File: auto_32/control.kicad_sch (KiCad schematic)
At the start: 12 parts, among them SW1 SW_Push, Y1 Crystal

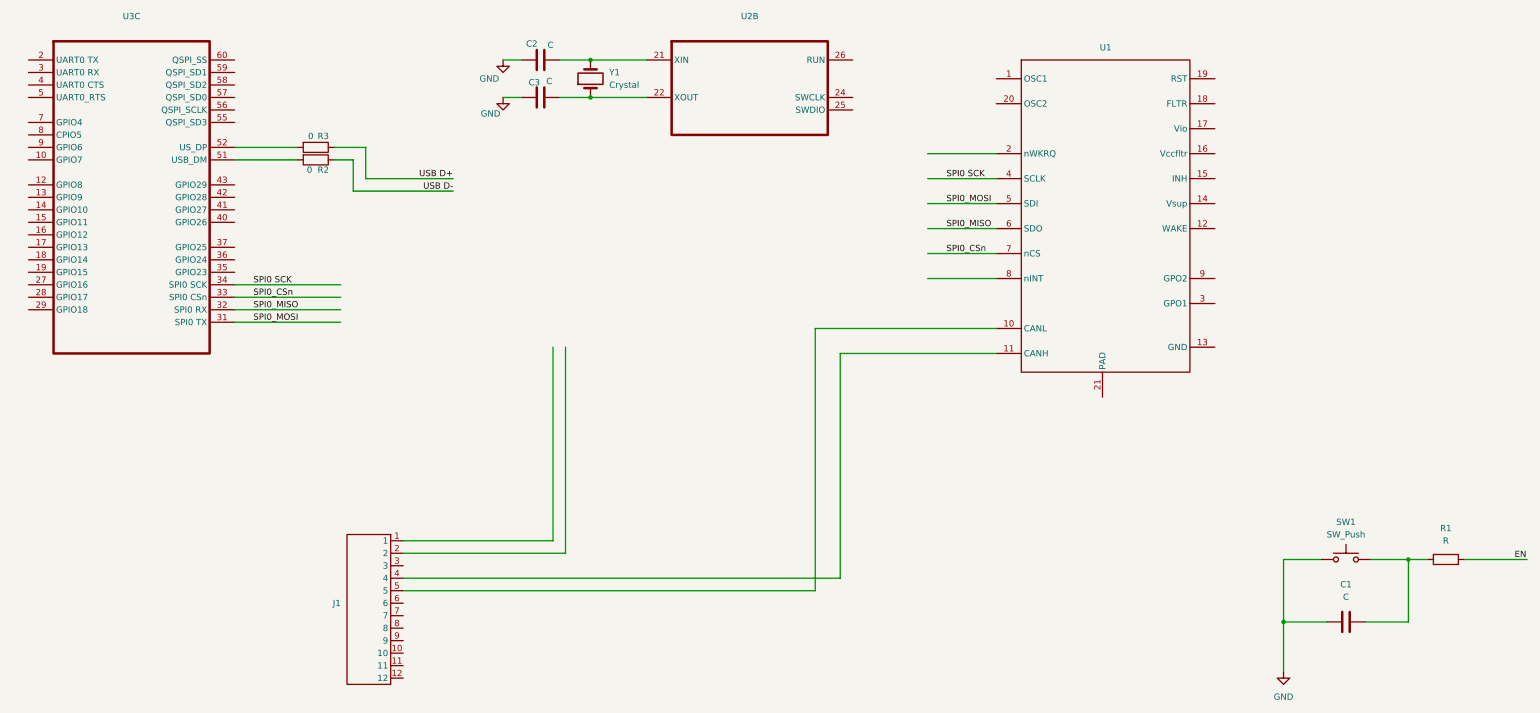
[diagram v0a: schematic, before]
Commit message: esp wroom reintroduced and can phy layer chip added
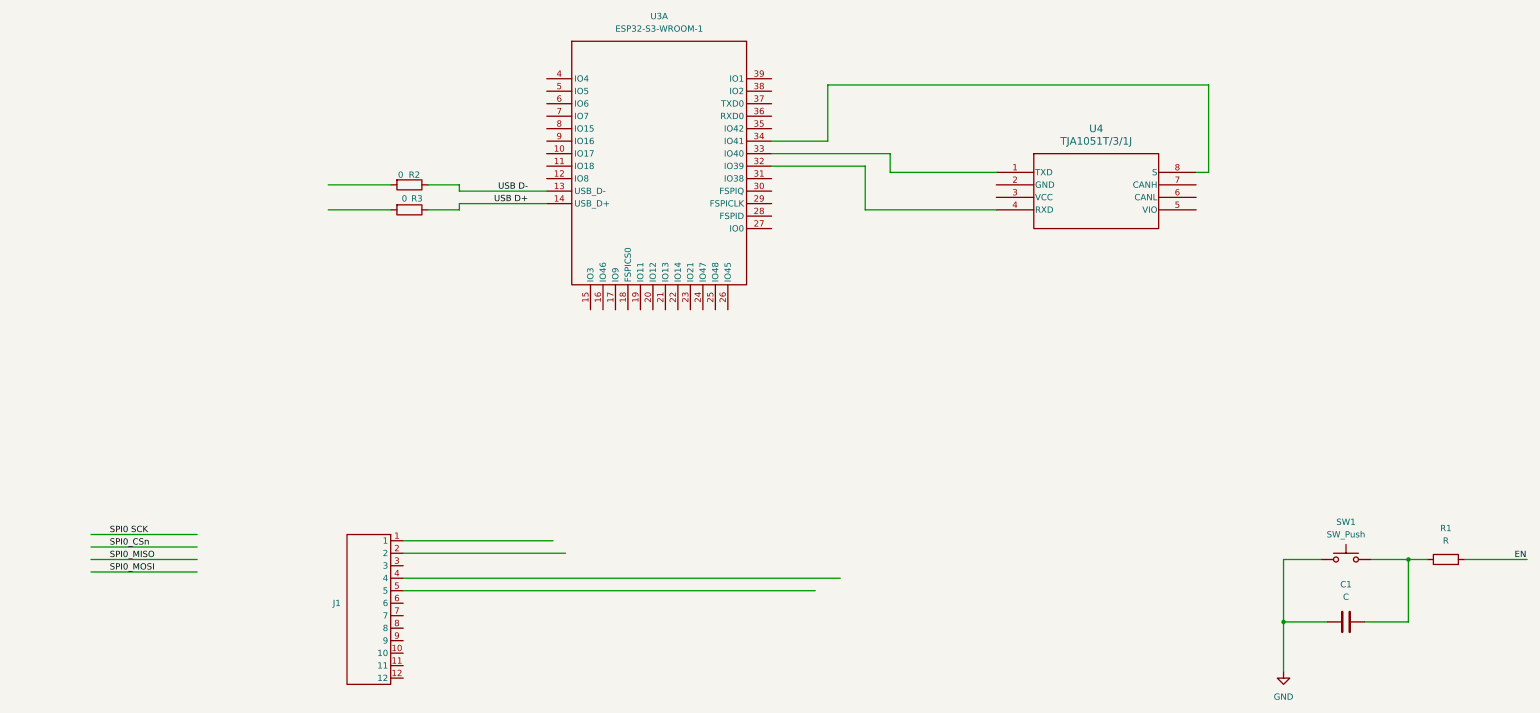
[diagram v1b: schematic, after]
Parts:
- removed C2: C, Capacitor_SMD:C_0603_1608Metric, symbol Device:C
- removed C3: C, symbol Device:C
- removed U1: ~, ssh_Library:VQFN-26_EP_3.5x4.5_Pitch0.5mm, symbol ssh_Library:TCAN4551RGYRQ1
- removed U2, U3: ~, ssh_IC_FP:RP2350A_QFN-60_EP_7.75x7.75_Pitch0.4mm, symbol ssh_IC_Lib:rp2050A_60pin
- removed Y1: Crystal, symbol Device:Crystal
- added U3: ESP32-S3-WROOM-1, RF_Module:ESP32-S3-WROOM-1, symbol ssh_Library:ESP32-S3-WROOM-1
- added U4: TJA1051T/3/1J, ssh_IC_FP:SO8_SOT96-1_NXP, symbol ssh_IC_Lib:TJA1051T_3_1J
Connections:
- net USB D+: now also U3.14 (IO20)
- net USB D-: now also U3.13 (IO19)
- new net: U3.32 (IO39), U4.4 (RXD)
- new net: U3.33 (IO40), U4.1 (TXD)
- new net: U3.34 (IO41), U4.8 (S)
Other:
- moved on the sheet: R2, R3

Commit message: march update
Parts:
- removed C1: C, symbol Device:C
- removed R1: R, symbol Device:R
- removed SW1: SW_Push, symbol Switch:SW_Push
- added C?: 4n7F, symbol Device:C
- added R? (x2): 60R, symbol Device:R
- renumbered R2 to R4, R3 to R5, U3 to U2, U4 to U3
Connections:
- net GND: now also U3.2 (GND), C?.2
- net CANH: now reaches J1.4
- net CANH: now also U3.7 (CANH), R?.2
- net CANL: now reaches J1.5
- net CANL: now also U3.6 (CANL), R?.1
- net +5V: now reaches U3.3 (VCC)
- net +3.3V: now reaches U3.5 (VIO)
- new net: C?.1, R?.1, R?.2
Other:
- moved on the sheet: R4, R5, U2A, U3
